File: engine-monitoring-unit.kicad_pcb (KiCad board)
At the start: 4 copper layers, 70 x 50 mm, 60 parts, among them J1 SW Debug, J2 Supply, J3 Oil Temperature, J4 Air Temperature, J5 Wheel Speed, J6 Inductive Sensor Wire, Q1 MMBT3904, SW1 KEY, SW2 BOOT, SW3 RST, U1 LMR16006XDDCR, U2 STM32F411CEU6, Y1 HSE, Y2 LSE

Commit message: Updated Footprint for swd
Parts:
- J1: footprint Connector_PinHeader_1.00mm:PinHeader_1x04_P1.00mm_Vertical -> Connector_PinHeader_2.54mm:PinHeader_1x04_P2.54mm_Vertical
- moved J1 4.75 mm to (187.6, 140.0)
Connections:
- U2 pad 50: GND -> (no net)
- U2 pad 51: GND -> (no net)
- U2 pad 52: GND -> (no net)
- U2 pad 53: GND -> (no net)
- U2 pad 54: GND -> (no net)
- U2 pad 55: GND -> (no net)
- U2 pad 56: GND -> (no net)
- U2 pad 57: GND -> (no net)
- U2 pad 58: GND -> (no net)
- U2 pad 59: GND -> (no net)
- U2 pad 60: GND -> (no net)
- U2 pad 61: GND -> (no net)
- U2 pad 62: GND -> (no net)
- U2 pad 63: GND -> (no net)
- U2 pad 64: GND -> (no net)
- U2 pad 65: GND -> (no net)
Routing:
- net +3.3V: track 245.3 -> 242.7 mm
- net /PA13: track 34.8 -> 33.5 mm
- net /PA14: track 45.4 -> 44.7 mm
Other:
- board text added: "3.3V"
- board text added: "SWCLK"
- board text added: "SWDIO"

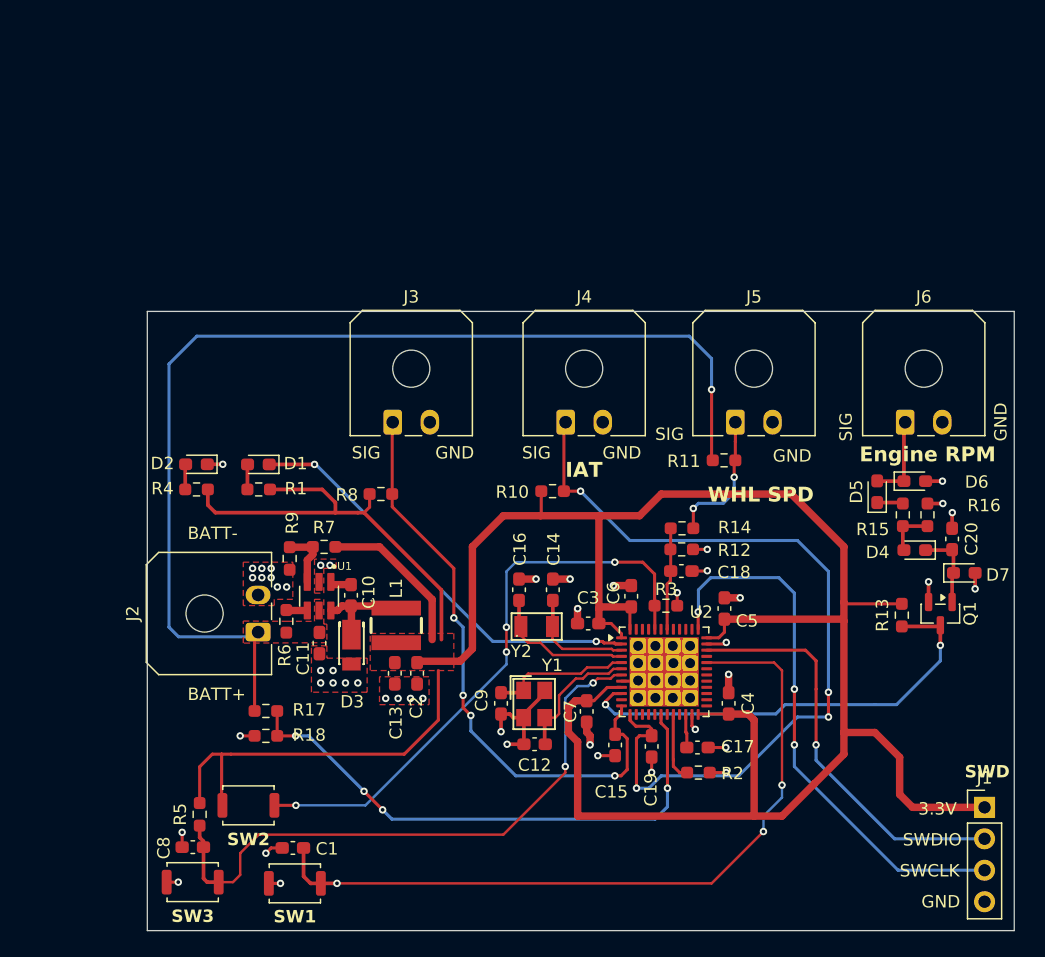
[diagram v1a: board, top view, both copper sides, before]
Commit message: Updated Silkscreen
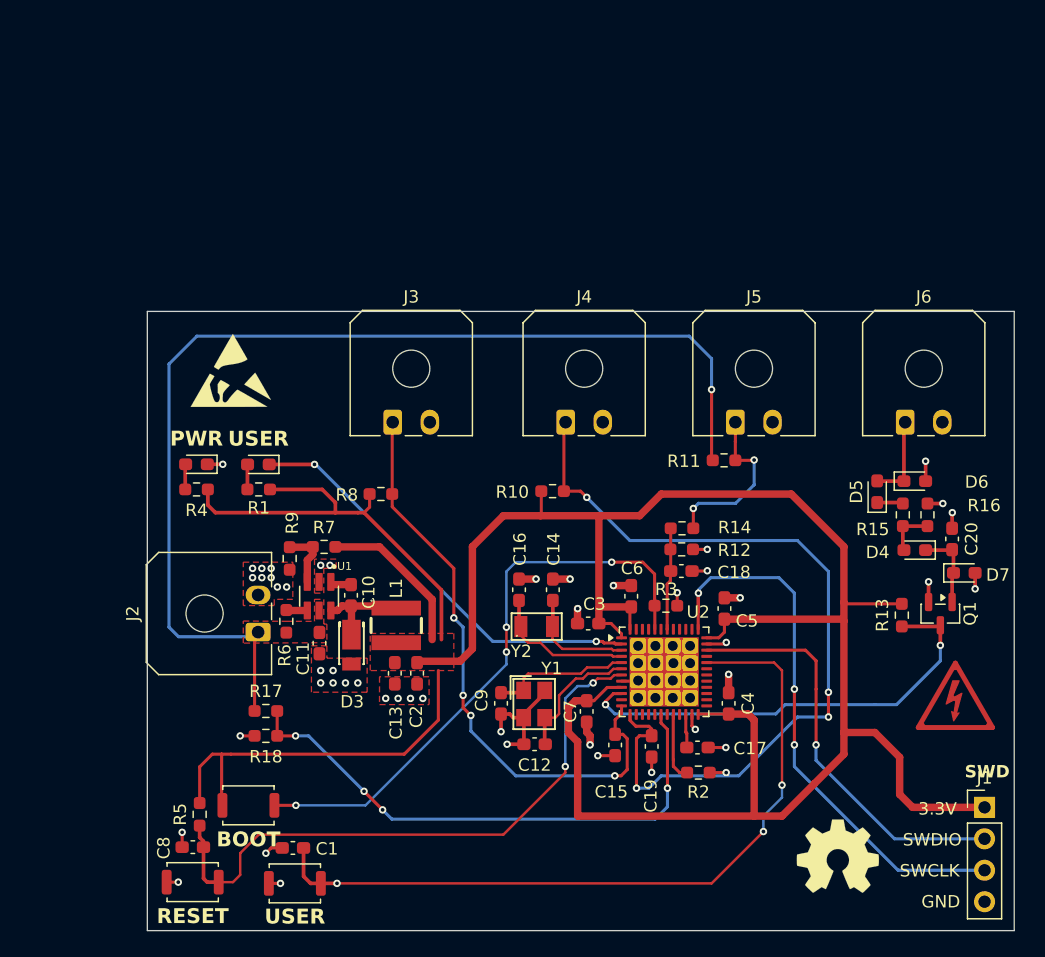
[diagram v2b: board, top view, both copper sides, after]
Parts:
- added REF**: ESD-Logo_6.6x6mm_SilkScreen, Symbol:ESD-Logo_6.6x6mm_SilkScreen, F.Cu at (126.8, 104.8)
- added REF**: Symbol_HighVoltage_Triangle_6x6mm_Copper, Symbol:Symbol_HighVoltage_Triangle_6x6mm_Copper, F.Cu at (185.2, 131.0)
- added REF**: OSHW-Symbol_6.7x6mm_SilkScreen, Symbol:OSHW-Symbol_6.7x6mm_SilkScreen, F.Cu at (175.8, 144.0)
- renumbered SW2 to BOOT, D2 to PWR, SW3 to RESET, SW1 to USER, D1 to USER
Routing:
- net Net-(J5-Pin_1): track 11.1 -> 14.0 mm
- net /PA14: track 44.7 -> 46.2 mm
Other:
- board text added: "ENGINE MONITORING UNIT"
- board text added: "ENGINE RPM"
- board text added: "OIL TEMP"
- board text added: "POWER"
- board text added: "WHEEL SPD"
- board text removed: "Engine RPM"
- board text removed: "Oil Temp"
- board text removed: "WHL SPD"

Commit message: Added Silkscreen Detaisls
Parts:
- moved C7 25.0 mm to (145.7, 109.3)
- moved R2 25.0 mm to (154.8, 114.2)
- moved R5 25.0 mm to (114.5, 117.6)
- moved RESET 25.0 mm to (113.9, 123.1)
- moved D3 25.0 mm to (126.7, 104.3)
- moved C11 25.0 mm to (124.2, 103.8)
- moved C13 25.0 mm to (130.2, 106.2)
- moved C14 25.0 mm to (143.0, 99.5)
- moved C16 25.0 mm to (140.3, 99.5)
- moved C17 25.0 mm to (154.7, 112.2)
- moved C18 25.0 mm to (153.4, 98.0)
- moved C19 25.0 mm to (151.0, 112.1)
- moved C2 25.0 mm to (132.0, 106.2)
- moved C20 25.0 mm to (175.2, 95.4)
- moved C3 25.0 mm to (145.8, 102.2)
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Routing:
- net /PA3: track 67.7 -> 68.5 mm
- net GND: track 49.7 -> 49.1 mm

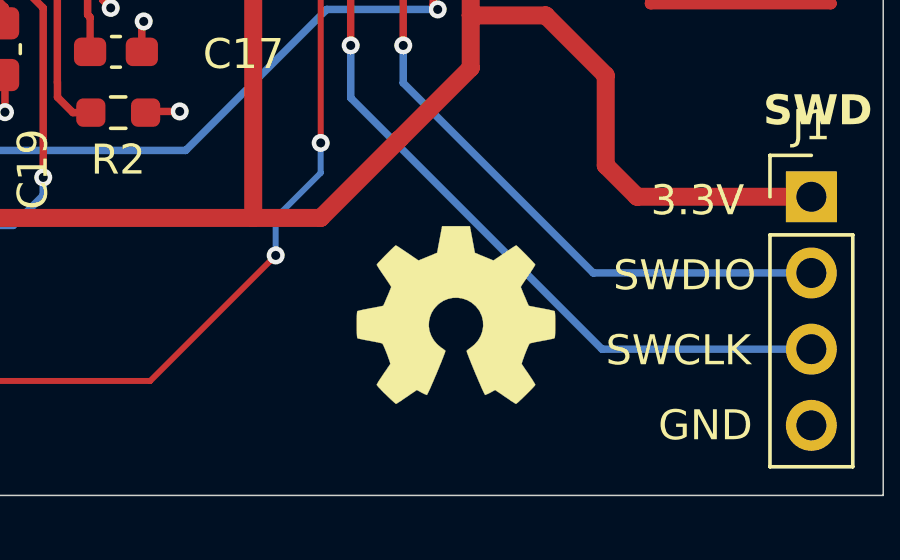
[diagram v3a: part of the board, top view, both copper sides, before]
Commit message: Added Silkscreen Details
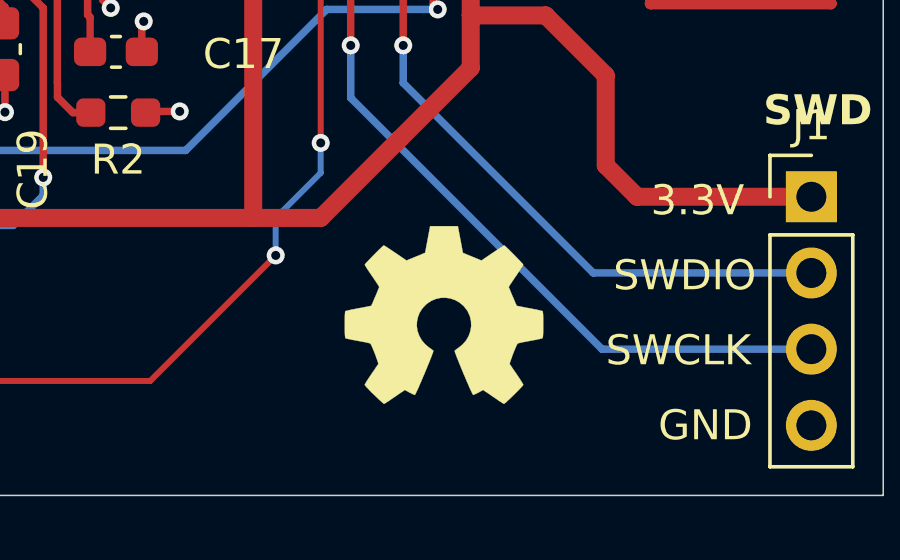
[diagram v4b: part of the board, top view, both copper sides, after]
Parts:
- moved REF** 0.40 mm to (165.6, 121.0)

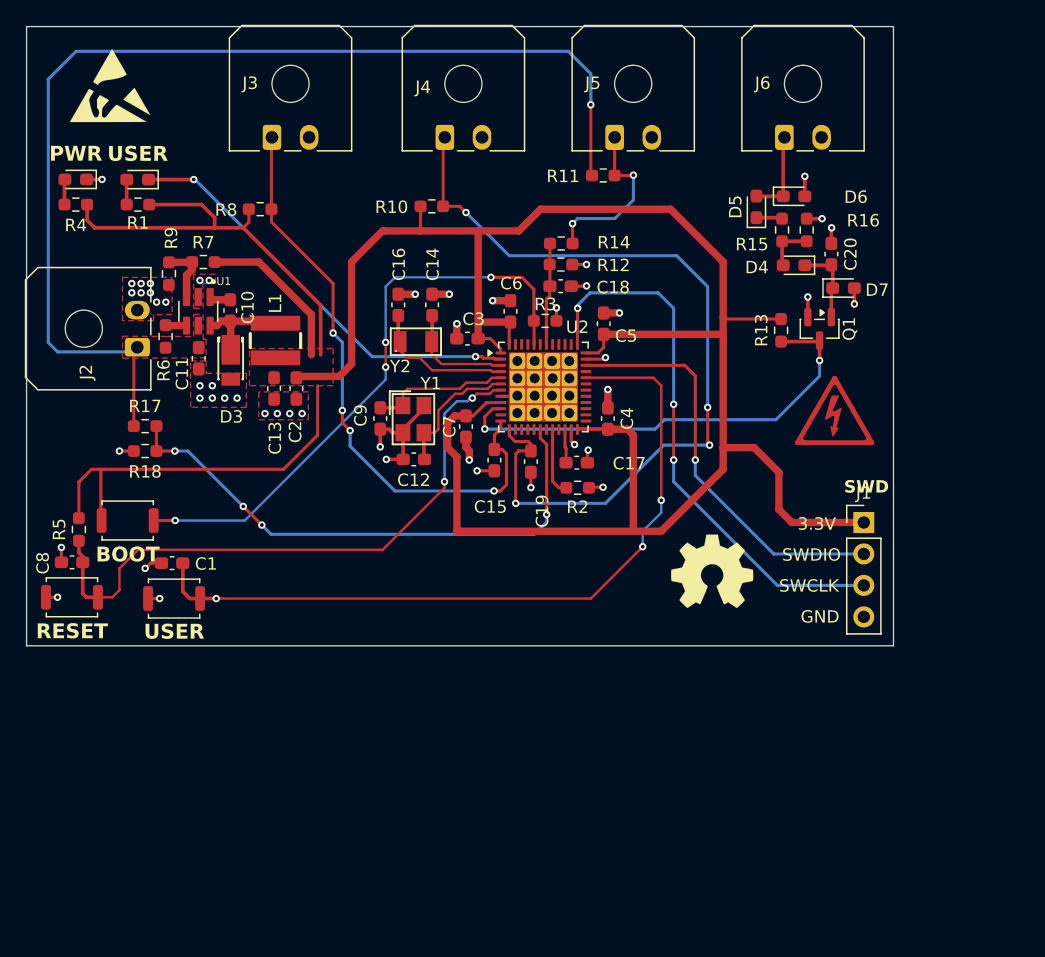
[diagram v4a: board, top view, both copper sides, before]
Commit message: Added OLED Display Socket
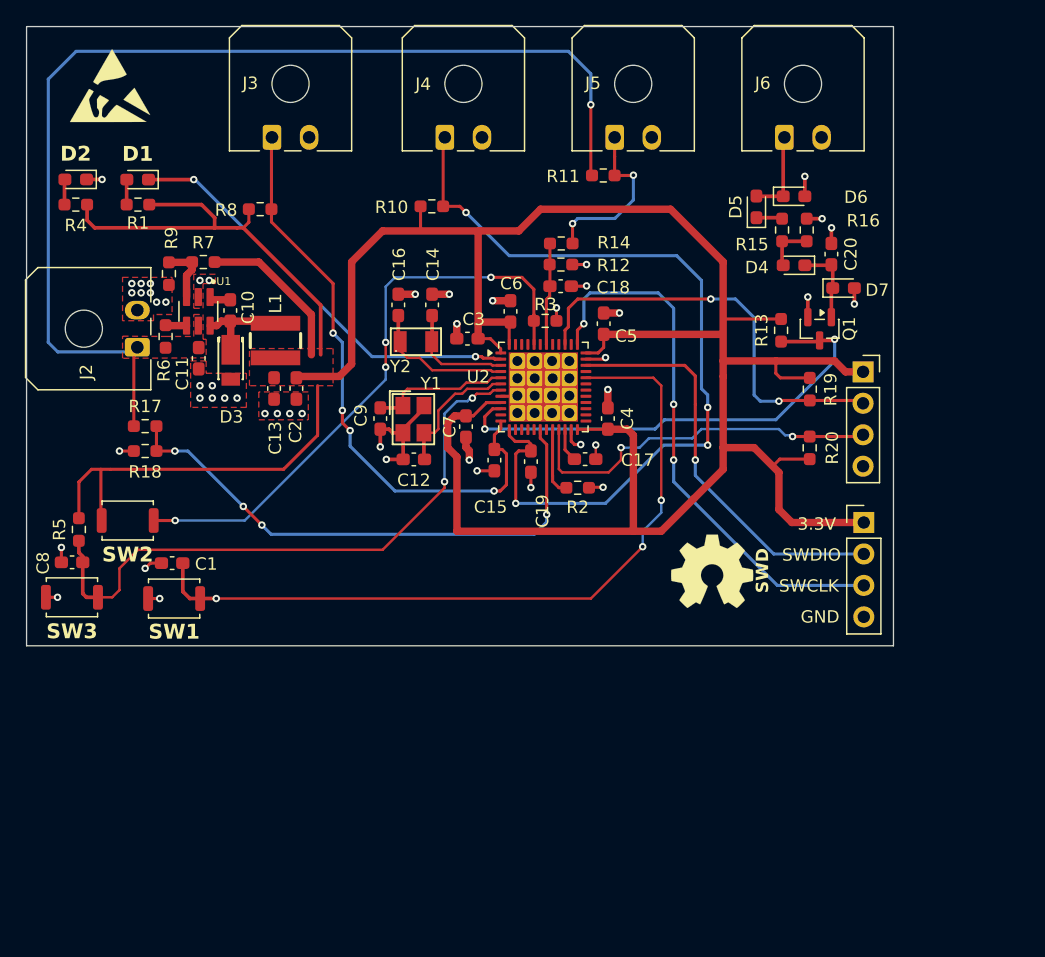
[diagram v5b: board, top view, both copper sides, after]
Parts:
- removed the REF** at (175.5, 108.0)
- added J7: SW Debug, Connector_PinSocket_2.54mm:PinSocket_1x04_P2.54mm_Vertical, F.Cu at (177.8, 104.9)
- added R19: 2.2K, Resistor_SMD:R_0603_1608Metric_Pad0.98x0.95mm_HandSolder, F.Cu at (173.5, 106.3)
- added R20: 2.2K, Resistor_SMD:R_0603_1608Metric_Pad0.98x0.95mm_HandSolder, F.Cu at (173.5, 111.0)
- moved C17 0.73 mm to (155.3, 111.9)
- renumbered USER to D1, PWR to D2, USER to SW1, BOOT to SW2, RESET to SW3
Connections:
- U2 pad 21: unconnected-(U2-PB10-Pad21) -> /PB10
- U2 pad 39: unconnected-(U2-PB3-Pad39) -> /PB3
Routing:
- net /PB3: track 0.00 -> 34.3 mm, vias 0 -> 2
- net /PB10: track 0.00 -> 30.2 mm, vias 0 -> 2
- net +3.3V: track 242.7 -> 261.5 mm
- net /PA0: track 37.2 -> 39.1 mm
- net /PA14: track 46.2 -> 44.7 mm
- net GND: track 49.1 -> 49.7 mm
